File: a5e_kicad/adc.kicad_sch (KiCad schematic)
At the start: 18 parts, among them U3 SN74LV4051APWR, U4 OPA365AIDBVR, U5 ADS7056IRUGR

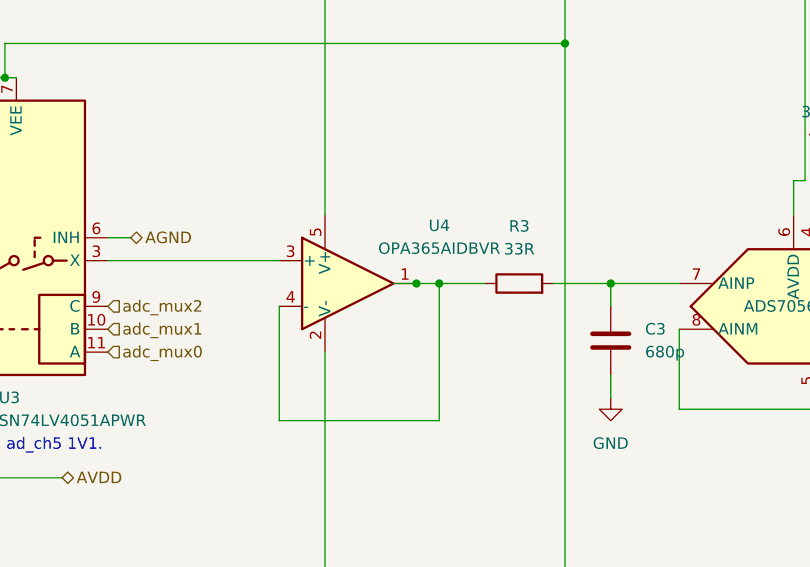
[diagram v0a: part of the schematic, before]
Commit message: Schematic reorg step 9: ERC to zero
- Wires trimmed back to their last label or cap (SDM config lines, LPDDR4
  decoupling rows, PG pins); loose stubs and R29 leftovers removed
- Unused bus links removed: {iob6a}, {iobank_2aB}, {iob6c}, {phy} and the
  io_headers {jtag} (sheet pins, root buses, unnamed internal buses);
  {iob6b} bus tail trimmed

Netdiff: 0 renamed, 0 connectivity diffs. ERC 21 -> 0. PCB unchanged, DRC parity 0.
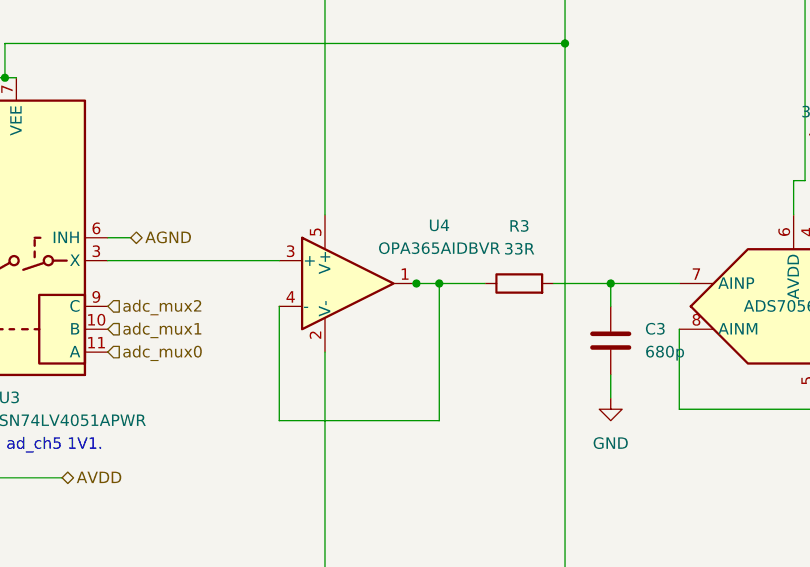
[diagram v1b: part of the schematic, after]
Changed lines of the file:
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@@
-	(wire
-		(pts
-			(xy 138.43 91.44) (xy 135.89 91.44)
-		)
-		(stroke
-			(width 0)
-			(type default)
-		)
-	)
 	(wire
 		(pts

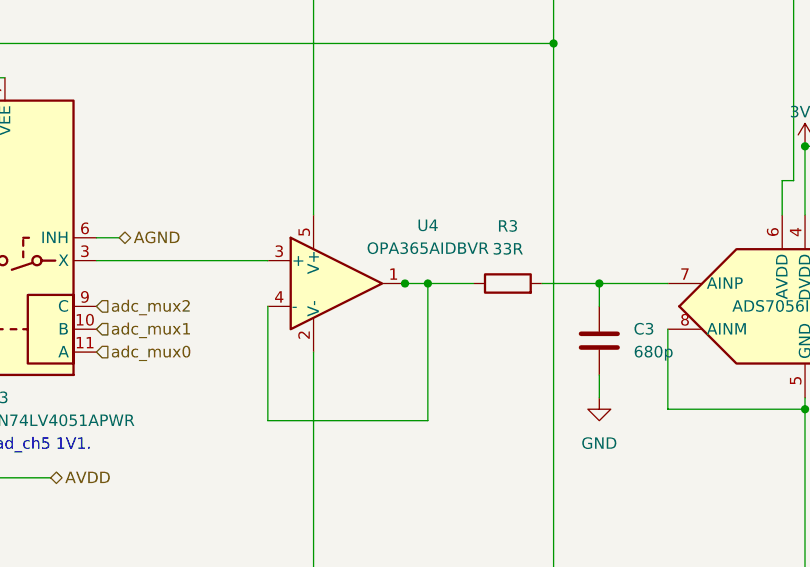
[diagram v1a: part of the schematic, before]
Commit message: Ethernet PHY passives to 0201, R27/R28 to 0402, preliminary RGMII routing
- 31 PHY passives on the hps_ethernet sheet 0402 -> 0201 (C24 22u stays
  0402): 100n C190183, 1u C272877, 27p C85899, 10k C473048,
  330R C516485, 4K7 C270346, 1K5 C270361, 2K49 C473476.
- Refclk bias R27/R28 0201 -> 0402 (C25120, 49.9R); R28 moved 0.1 mm
  to +x to clear the refclk_N meander.
- Preliminary RGMII routing: RX on F.Cu, TX on In2. Group spread
  TX 79 ps (TXD1 longest), RX 44 ps.
- Schematic sheets as saved by eeschema.
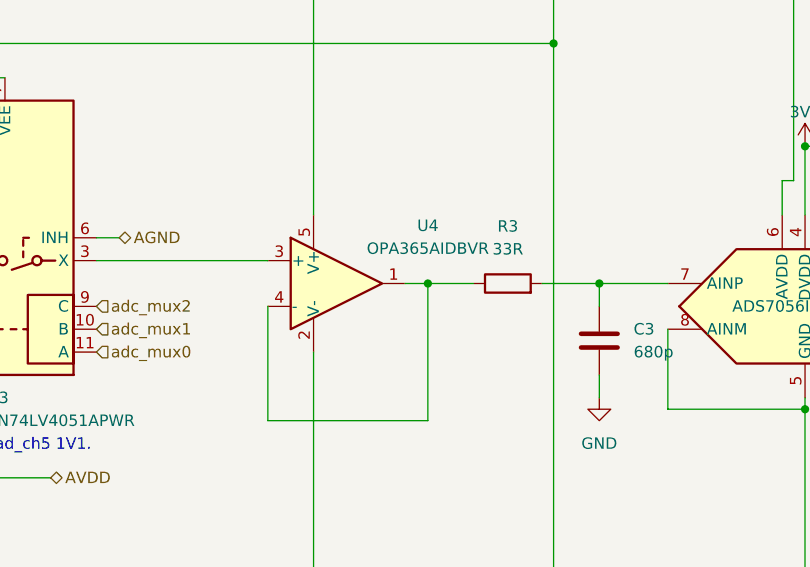
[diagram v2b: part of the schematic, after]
